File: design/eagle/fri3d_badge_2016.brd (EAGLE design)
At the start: 76.6 x 67.3 mm, 43 parts, among them Q1 MOSFET-NCHANNEL2N7002PW, U1 MCP73831

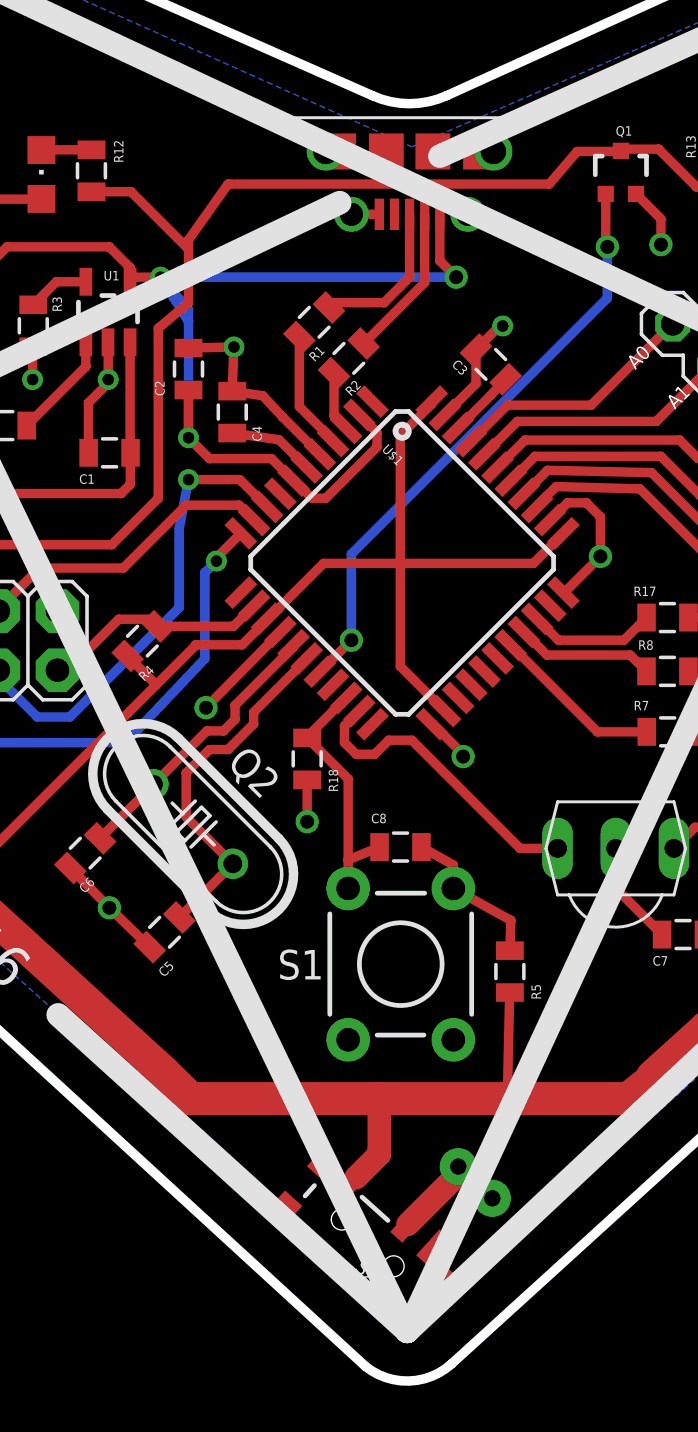
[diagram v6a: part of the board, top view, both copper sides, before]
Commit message: fixed switch footprint
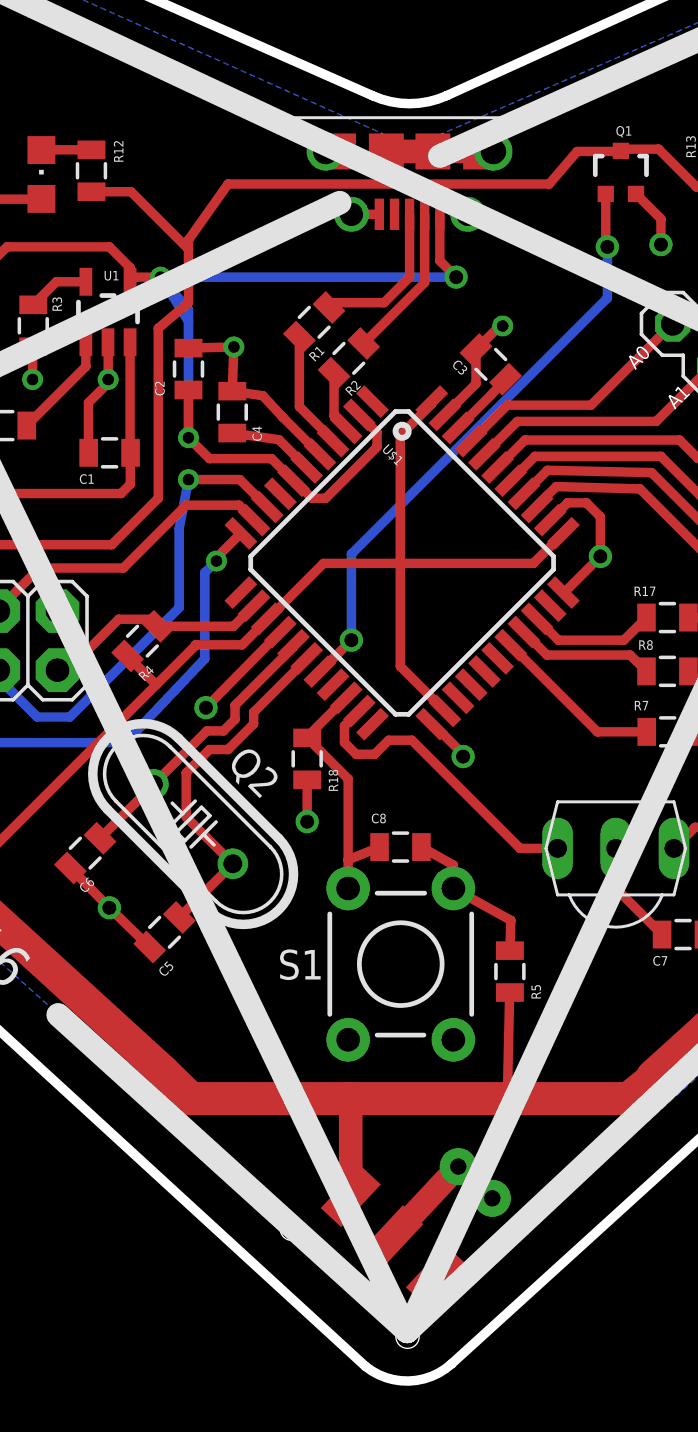
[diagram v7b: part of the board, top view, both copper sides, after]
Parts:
- removed S2: (no value), SparkFun-Electromechanical:SWITCH-SPST-SMD-A
- added U$6: SLIDE-SWITCH, FriedCamp:SLIDE-SWITCH
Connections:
- net N$17: now also U$6.K; no longer S2.2
- net VCC: now also U$6.K2; no longer S2.3
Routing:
- net GND: track 48.4 -> 53.5 mm
- net N$17: track 3.35 -> 4.09 mm
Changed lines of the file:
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@@
 <attribute name="VALUE" x="36.503" y="28.316" size="0.4064" layer="27" rot="R270"/>
-</element>
-<element name="S2" library="SparkFun-Electromechanical" package="SWITCH-SPST-SMD-A" value="" x="38.2" y="6.4" rot="R138">
-<attribute name="PROD_ID" value="SWCH-10651" x="38.2" y="6.4" size="1.778" layer="27" rot="R138" display="off"/>
 </element>
 <element name="U$4" library="Badge_EZR_V1" package="DRAGAN-PERSONAL_AVAGO-RGB-LED" value="DRAGAN-PERSONAL_AVAGO-RGB-LED" x="58.7" y="28.4" rot="R90"/>
 <element name="U$5" library="OCTA-EZR_v1" package="OCTA-CORE_MICRO-USB2" value="OCTA-CORE_MCIRO-USB2MOUSER" x="40" y="50.6" rot="R180"/>
+<element name="U$6" library="FriedCamp" package="SLIDE-SWITCH" value="SLIDE-SWITCH" x="39.3" y="6.7" rot="R317"/>
 </elements>
 <signals>
@@
 <contactref element="U$5" pad="P$5"/>
 <wire x1="38.7" y1="50.6" x2="37.5" y2="50.6" width="0.4064" layer="1"/>
-<wire x1="43.6" y1="53.3" x2="43.05" y2="53.3" width="0" layer="19" extent="1-1"/>
-<wire x1="36.95" y1="53.3" x2="36.4" y2="53.3" width="0" layer="19" extent="1-1"/>
-<wire x1="41" y1="53.3" x2="43.05" y2="53.3" width="0" layer="19" extent="1-1"/>
-<wire x1="39" y1="53.3" x2="41" y2="53.3" width="0" layer="19" extent="1-1"/>
+<wire x1="39" y1="53.3" x2="41" y2="53.3" width="1.016" layer="1"/>
+<wire x1="41" y1="53.3" x2="43.05" y2="53.3" width="1.016" layer="1"/>
+<wire x1="36.4" y1="53.3" x2="36.95" y2="53.3" width="1.016" layer="1"/>
+<wire x1="43.05" y1="53.3" x2="43.6" y2="53.3" width="1.016" layer="1"/>
 </signal>
 <signal name="D+">
@@
 <wire x1="55.49" y1="22.27" x2="55.49" y2="24.25" width="0.4064" layer="1"/>
 <wire x1="55.49" y1="24.25" x2="55.5" y2="24.26" width="0.4064" layer="1"/>
-<contactref element="S2" pad="3"/>
-<wire x1="30.6" y1="12.6" x2="38.7" y2="12.6" width="1.4224" layer="1"/>
+<wire x1="30.6" y1="12.6" x2="37.4" y2="12.6" width="1.4224" layer="1"/>
+<wire x1="37.4" y1="12.6" x2="44.2" y2="12.6" width="1.4224" layer="1"/>
 <wire x1="44.2" y1="12.6" x2="49.4" y2="12.6" width="1.4224" layer="1"/>
 <wire x1="49.4" y1="12.6" x2="50.43818125" y2="13.43818125" width="1.4224" layer="1"/>
@@
 <wire x1="16.4" y1="34.3" x2="17.766421875" y2="32.933578125" width="0.4064" layer="1"/>
 <wire x1="17.766421875" y1="32.933578125" x2="17.766421875" y2="31.733575" width="0.4064" layer="1"/>
-<wire x1="37.6989" y1="9.206046875" x2="38.7" y2="10.207146875" width="1.016" layer="1"/>
-<wire x1="38.7" y1="10.207146875" x2="38.7" y2="12.6" width="1.016" layer="1"/>
-<wire x1="38.7" y1="12.6" x2="44.2" y2="12.6" width="1.4224" layer="1"/>
 <wire x1="29.405165625" y1="13.765609375" x2="30.6" y2="12.6" width="1.4224" layer="1"/>
 <contactref element="U$4" pad="P$1"/>
 <wire x1="58.7" y1="28.4" x2="61.7708625" y2="28.4" width="0.4064" layer="1"/>
 <wire x1="61.7708625" y1="28.4" x2="64.06163125" y2="26.10923125" width="0.4064" layer="1"/>
+<contactref element="U$6" pad="K2"/>
+<wire x1="37.471615625" y1="8.40499375" x2="37.471615625" y2="12.528384375" width="1.016" layer="1"/>
+<wire x1="37.471615625" y1="12.528384375" x2="37.4" y2="12.6" width="1.016" layer="1"/>
 </signal>
 <signal name="N$5">
@@
 <wire x1="51.290125" y1="45.890125" x2="51.309871875" y2="45.890125" width="0.4064" layer="1"/>
 </signal>
-<signal name="N$17">
-<contactref element="J3" pad="2"/>
-<contactref element="S2" pad="2"/>
-<wire x1="39.928334375" y1="7.198653125" x2="41.99355" y2="9.26386875" width="1.016" layer="1"/>
-<wire x1="41.99355" y1="9.26386875" x2="42.09355" y2="9.679753125" width="0.4064" layer="1"/>
-</signal>
 <signal name="N$19">
 <contactref element="R8" pad="2"/>
@@
 <wire x1="36.74" y1="46.8" x2="36.53639375" y2="46.59639375" width="0.4064" layer="1"/>
 </signal>
+<signal name="N$17">
+<contactref element="J3" pad="2"/>
+<contactref element="U$6" pad="K"/>
+<wire x1="42.09355" y1="9.679753125" x2="42.079753125" y2="9.679753125" width="1.016" layer="1"/>
+<wire x1="42.079753125" y1="9.679753125" x2="39.3" y2="6.7" width="1.016" layer="1"/>
+</signal>
 </signals>

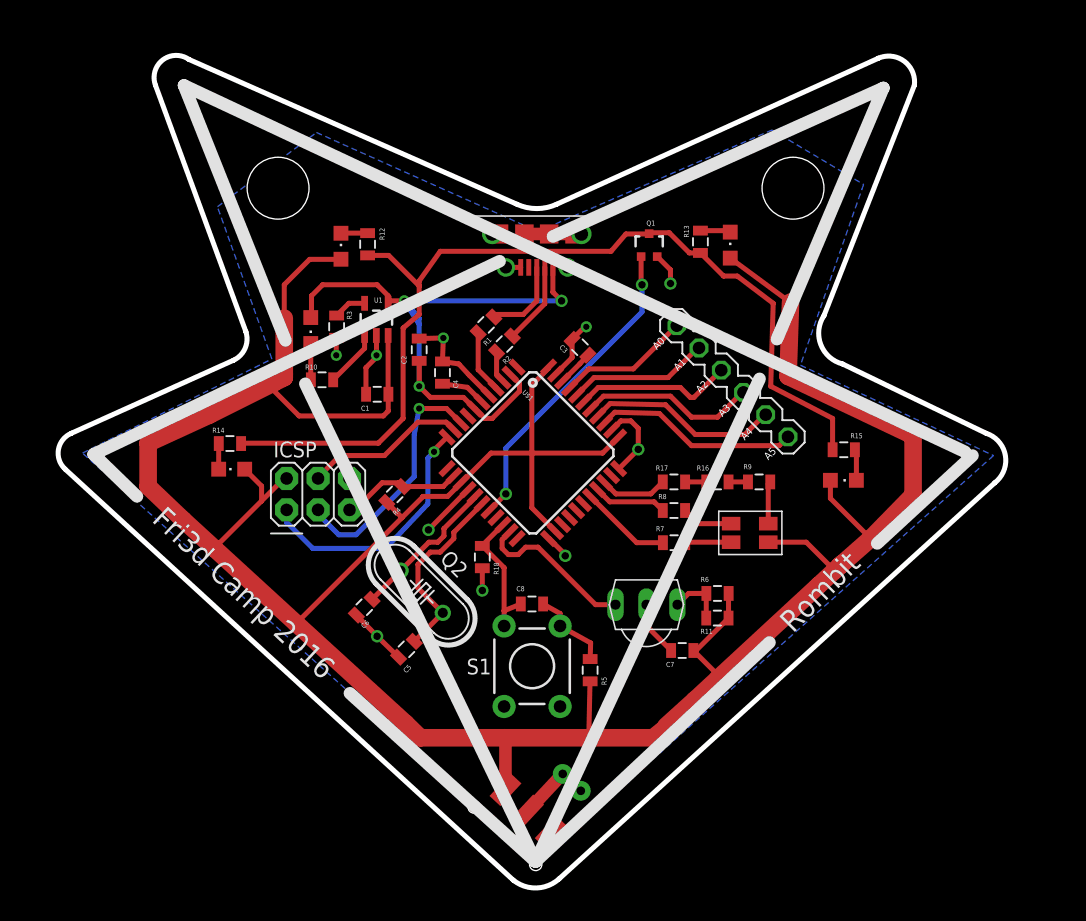
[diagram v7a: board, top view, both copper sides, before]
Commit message: replaced ICSP header with Tag Connect pads
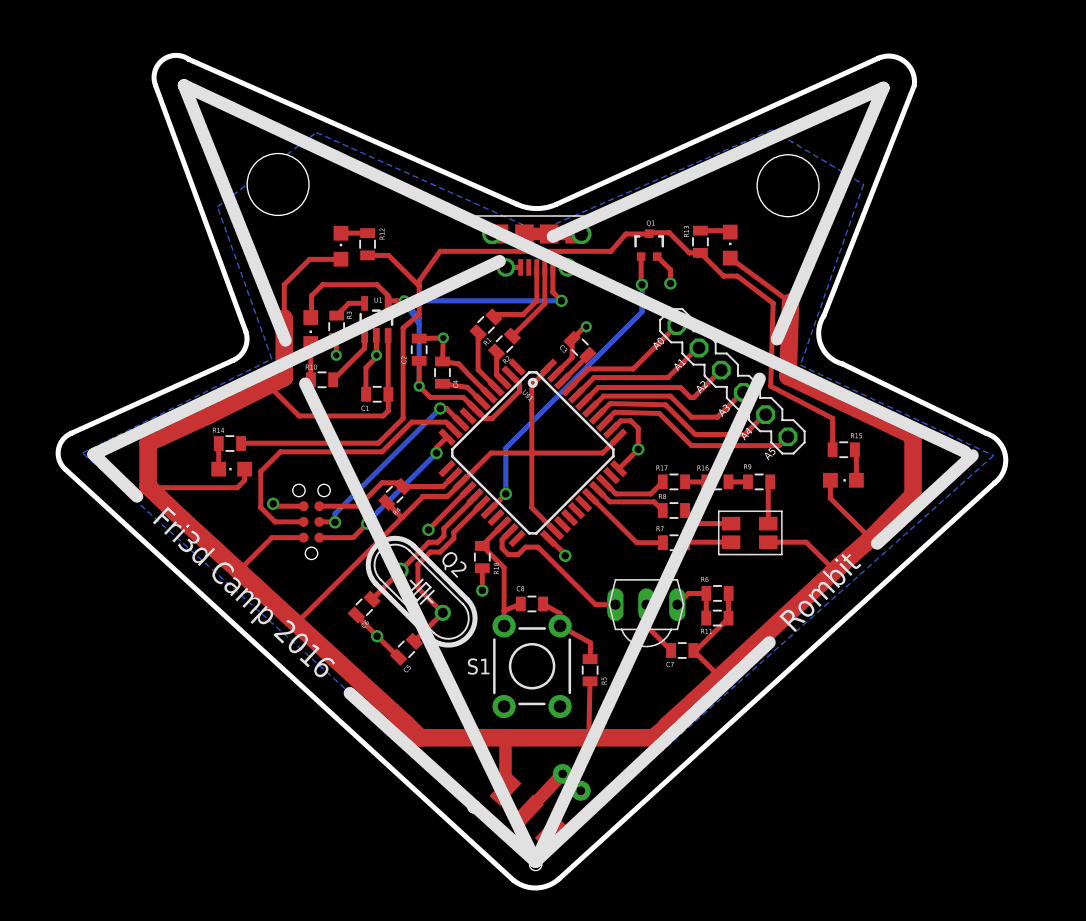
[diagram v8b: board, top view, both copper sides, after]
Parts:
- removed ICSP: (no value), SparkFun-Connectors:2X03
- added U$7: OCTA-CORE_TC2030-IDC, Badge_EZR_V1:OCTA-CORE_TC2030-IDC
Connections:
- net GND: now also U$7.P$4; no longer ICSP.6
- net MISO: now also U$7.P$1; no longer ICSP.1
- net MOSI: now also U$7.P$5; no longer ICSP.4
- net RST: now also U$7.P$3; no longer ICSP.5
- net SCK: now also U$7.P$2; no longer ICSP.3
- net VCC: now also U$7.P$6; no longer ICSP.2
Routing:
- net MOSI: track 13.2 -> 24.4 mm
- net MISO: track 21.0 -> 14.0 mm, vias 1 -> 2
- net VCC: track 243.7 -> 247.8 mm
- net SCK: track 20.2 -> 16.2 mm, vias 1 -> 2
- net GND: track 53.5 -> 56.1 mm, vias 10 -> 11
- net RST: track 9.85 -> 12.2 mm
